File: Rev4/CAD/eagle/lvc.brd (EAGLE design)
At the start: 31.8 x 31.8 mm, 26 parts, among them J1 3,5MM_1X2_SCREWTERM, J2 3,5MM_1X2_SCREWTERM, Q1 SI7997DP

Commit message: Updated voltage divider resistor values
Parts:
- R10: value 301k -> 1M
- R11: value 10k -> 100k
- R7: value 1.5M -> 1M
- R8: value 510k -> 1M
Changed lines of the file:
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@@
 <element name="J2" library="NR_conn" package="3.5MM_1X2" value="3,5MM_1X2_SCREWTERM" x="27.94" y="21.59" rot="R90"/>
 <element name="S1" library="NR_switch" package="CL-SB-13B" value="CL-SB-13B-02" x="20.32" y="9.8425" rot="R180"/>
-<element name="R7" library="resistor" package="R0603" value="1.5M" x="13.81125" y="7.064375"/>
-<element name="R8" library="resistor" package="R0603" value="510k" x="13.81125" y="5.55625" rot="R180"/>
+<element name="R7" library="resistor" package="R0603" value="1M" x="13.81125" y="7.064375"/>
+<element name="R8" library="resistor" package="R0603" value="1M" x="13.81125" y="5.55625" rot="R180"/>
 <element name="R9" library="resistor" package="R0603" value="1.5M" x="13.81125" y="2.54"/>
-<element name="R10" library="resistor" package="R0603" value="301k" x="13.81125" y="4.048125" rot="R180"/>
+<element name="R10" library="resistor" package="R0603" value="1M" x="13.81125" y="4.048125" rot="R180"/>
 <element name="VR1" library="NR_pot" package="J-LEAD_TOP_ADJ" value="BOURNS_3214W" x="29.05125" y="8.89" rot="R180"/>
-<element name="R11" library="resistor" package="R0603" value="10k" x="29.21" y="12.7"/>
+<element name="R11" library="resistor" package="R0603" value="100k" x="29.21" y="12.7"/>
 <element name="TP1" library="CM_test" package="TP_2.5MM" value="TESTPOINT" x="29.21" y="15.24"/>
 <element name="S2" library="AR_switches" package="CL-SB-12B" value="CL-SB-12B-02" x="8.89" y="9.8425"/>

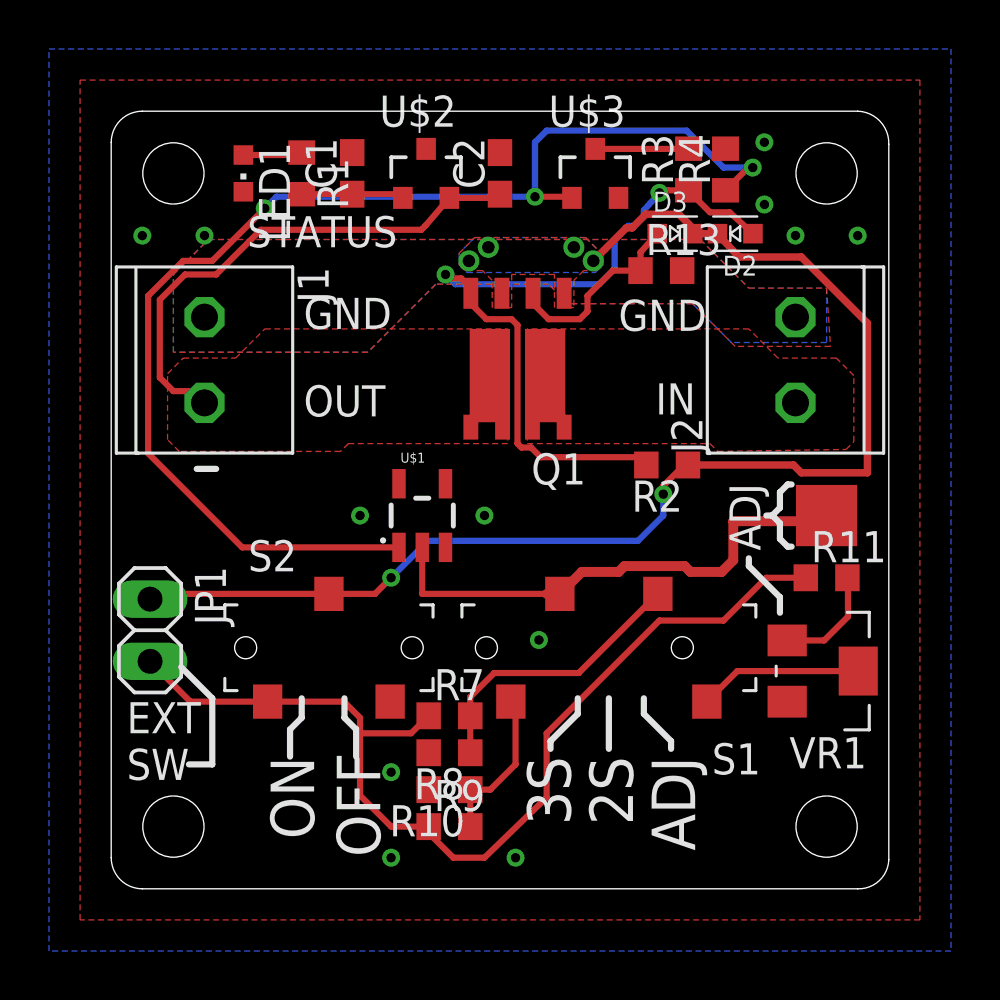
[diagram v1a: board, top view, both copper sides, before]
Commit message: Added comparator protection; cleaned up schematic
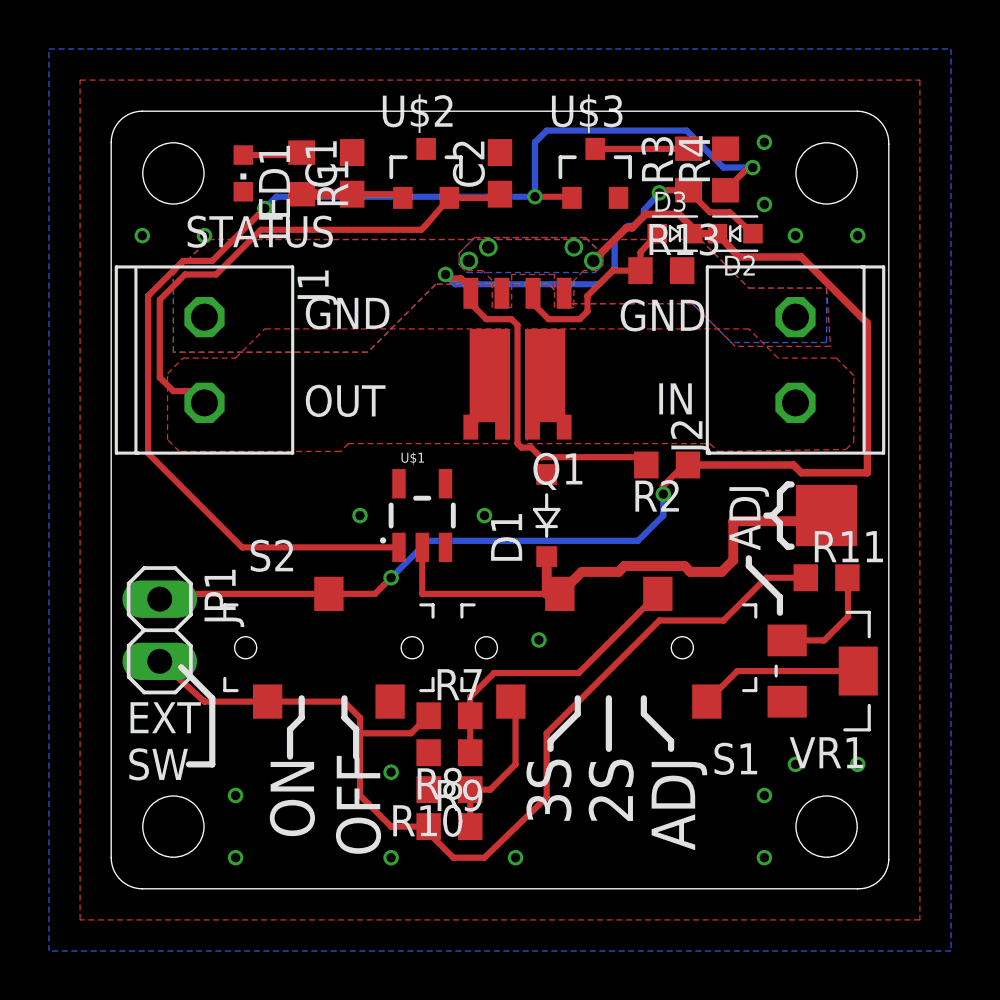
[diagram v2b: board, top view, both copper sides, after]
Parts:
- added D1: BZT52B8V2, vishay1:SOD123
- R11: value 100k -> 10k
- R9: value 1.5M -> 2M
- moved JP1 0.40 mm to (1.98, 10.6)
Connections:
- net N$2 renamed LED
- net GND: now also D1.A
- net V_DIV: now also D1.C
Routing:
- net V_DIV: track 20.9 -> 22.4 mm
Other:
- board text added: "4.5-28V In 5A Max"
- board text added: "LVC Rev 4"
- board text removed: "3-28V In 10A Max"
- board text removed: "Cutoff On Off"
- board text removed: "Green Blinking"
- board text removed: "LVC Rev 3"
- board text removed: "No Lights"
- board text removed: "Red Blinking"

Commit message: Added Rev4 final
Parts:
- removed R11: 10k, resistor:R0603
- removed R13: 1M, resistor:R0603
- removed U$2: TLV76033DBZR, rohm1:SOT23
- added R5, R6: 1M, resistor:R0603
- added U1: L78L33ACUTR, LR_vreg:SOT-89
- C1: value 0.1uF -> 0.33uF
- C2: value 0.33uF -> 0.1uF
- R7: value 1M -> 2M
- R9: value 2M -> 10k
- moved R10 22.9 mm to (22.5, 25.2), turned to 0 degrees
- moved R9 18.4 mm to (29.2, 12.7)
- moved R7 4.52 mm to (13.8, 2.54)
- moved U$1 3.81 mm to (16.5, 15.2)
- moved C1 3.77 mm to (6.59, 27.3), turned to 270 degrees
- moved R1 2.56 mm to (10.2, 30.2), turned to 0 degrees
- moved D1 2.54 mm to (20.3, 15.2)
- moved C2 2.06 mm to (14.0, 30.2), turned to 0 degrees
- moved R8 1.51 mm to (13.8, 4.05)
- moved LED1 1.40 mm to (6.43, 30.2), turned to 90 degrees
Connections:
- net 2_CELL: now also R5.2, R6.1; no longer R7.2, R8.1
- net 3_CELL: now also R7.2, R8.1; no longer R10.1, R9.2
- net EN: now also R5.1; no longer R11.1
- net GND: now also R6.2, U1.2; no longer R13.2, U$2.3
- net LED: now also C2.1, U1.1; no longer C1.1, U$2.1
- net N$11: now also R9.2; no longer R11.2
- net N$6: now also R10.1; no longer R13.1
- net VOUT: now also C1.1, U1.3; no longer C2.1, U$2.2
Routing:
- net LOAD: track 51.1 -> 57.8 mm
- net VOUT: track 21.4 -> 15.5 mm
- net V_DIV: track 22.4 -> 18.1 mm
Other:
- board text added: "5-28V In 5A Max"
- board text removed: "4.5-28V In 5A Max"
- board text removed: "STATUS"
